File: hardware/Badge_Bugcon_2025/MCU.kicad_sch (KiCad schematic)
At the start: 62 parts, among them J1 Conn_01x21, J13 ETH, J14 Conn_01x24, J5 3V3, J8 Conn_01x24, SW2 SW_Push, SW3 SW_Push, U6 W25N02KVZEIR, Y1 Crystal, Y2 24MHz

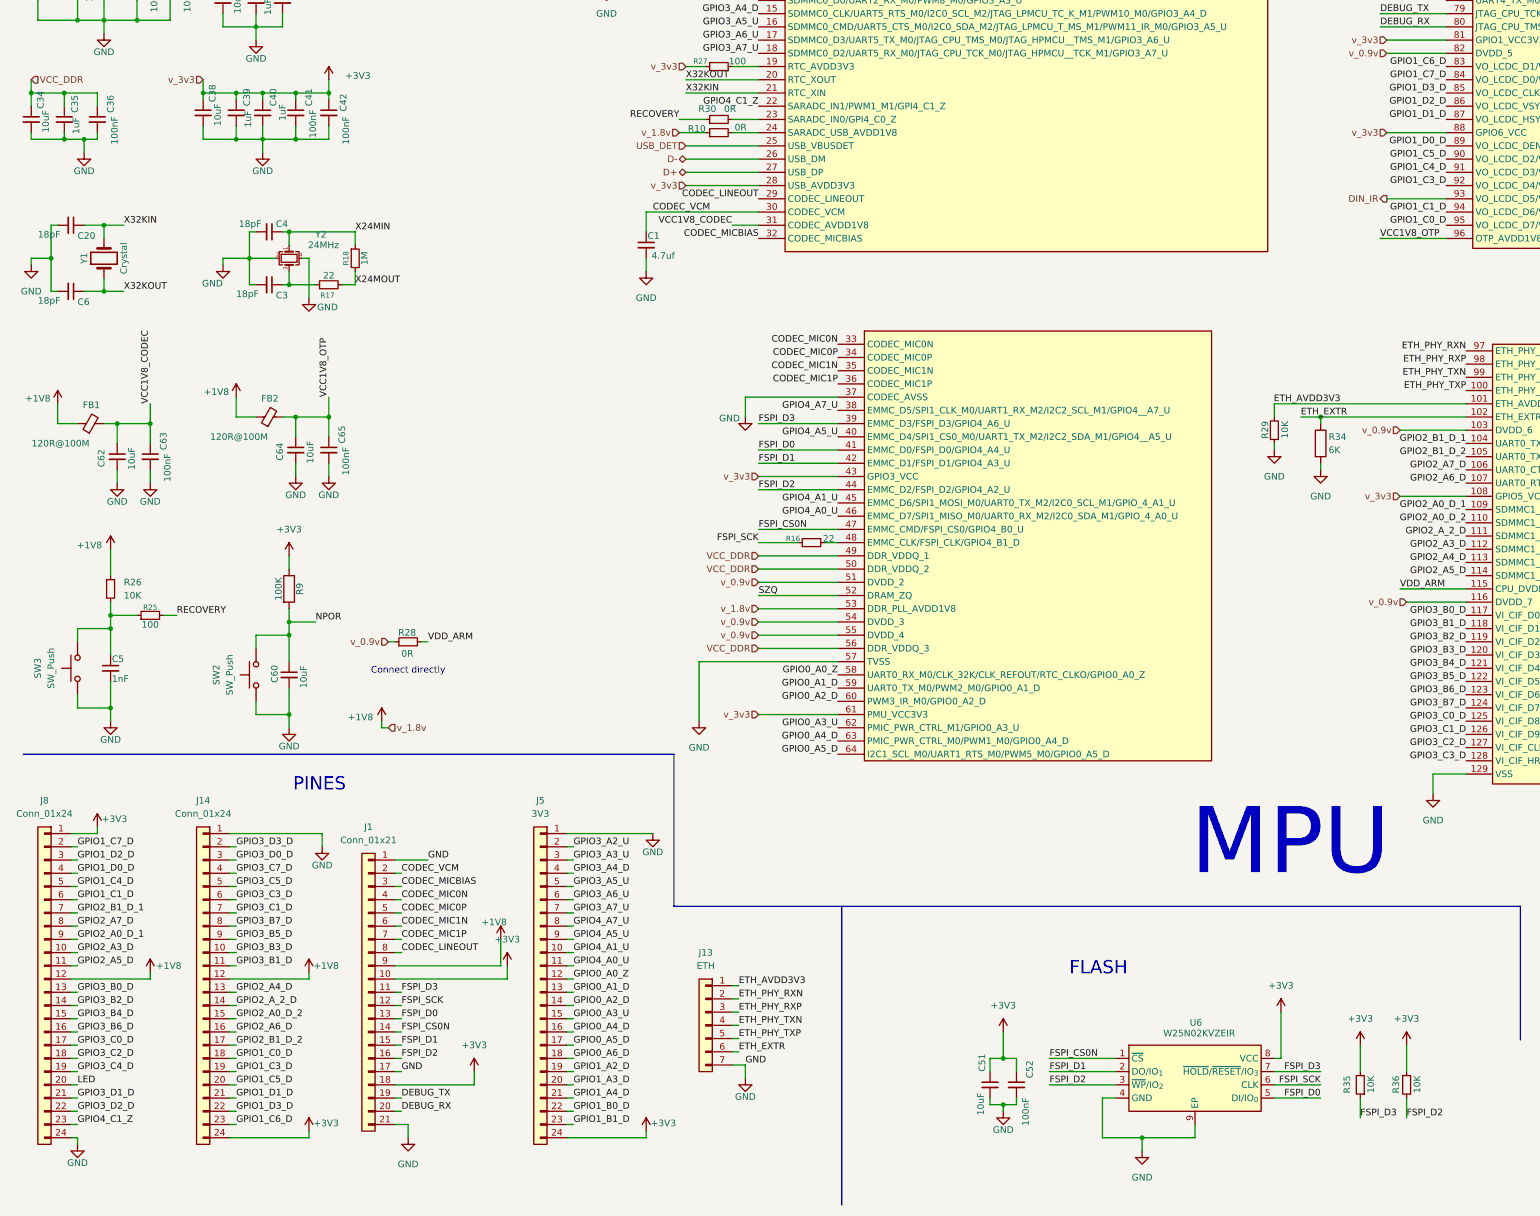
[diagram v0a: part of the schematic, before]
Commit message: feat(Hw):Update_Schaematic_And_BOM
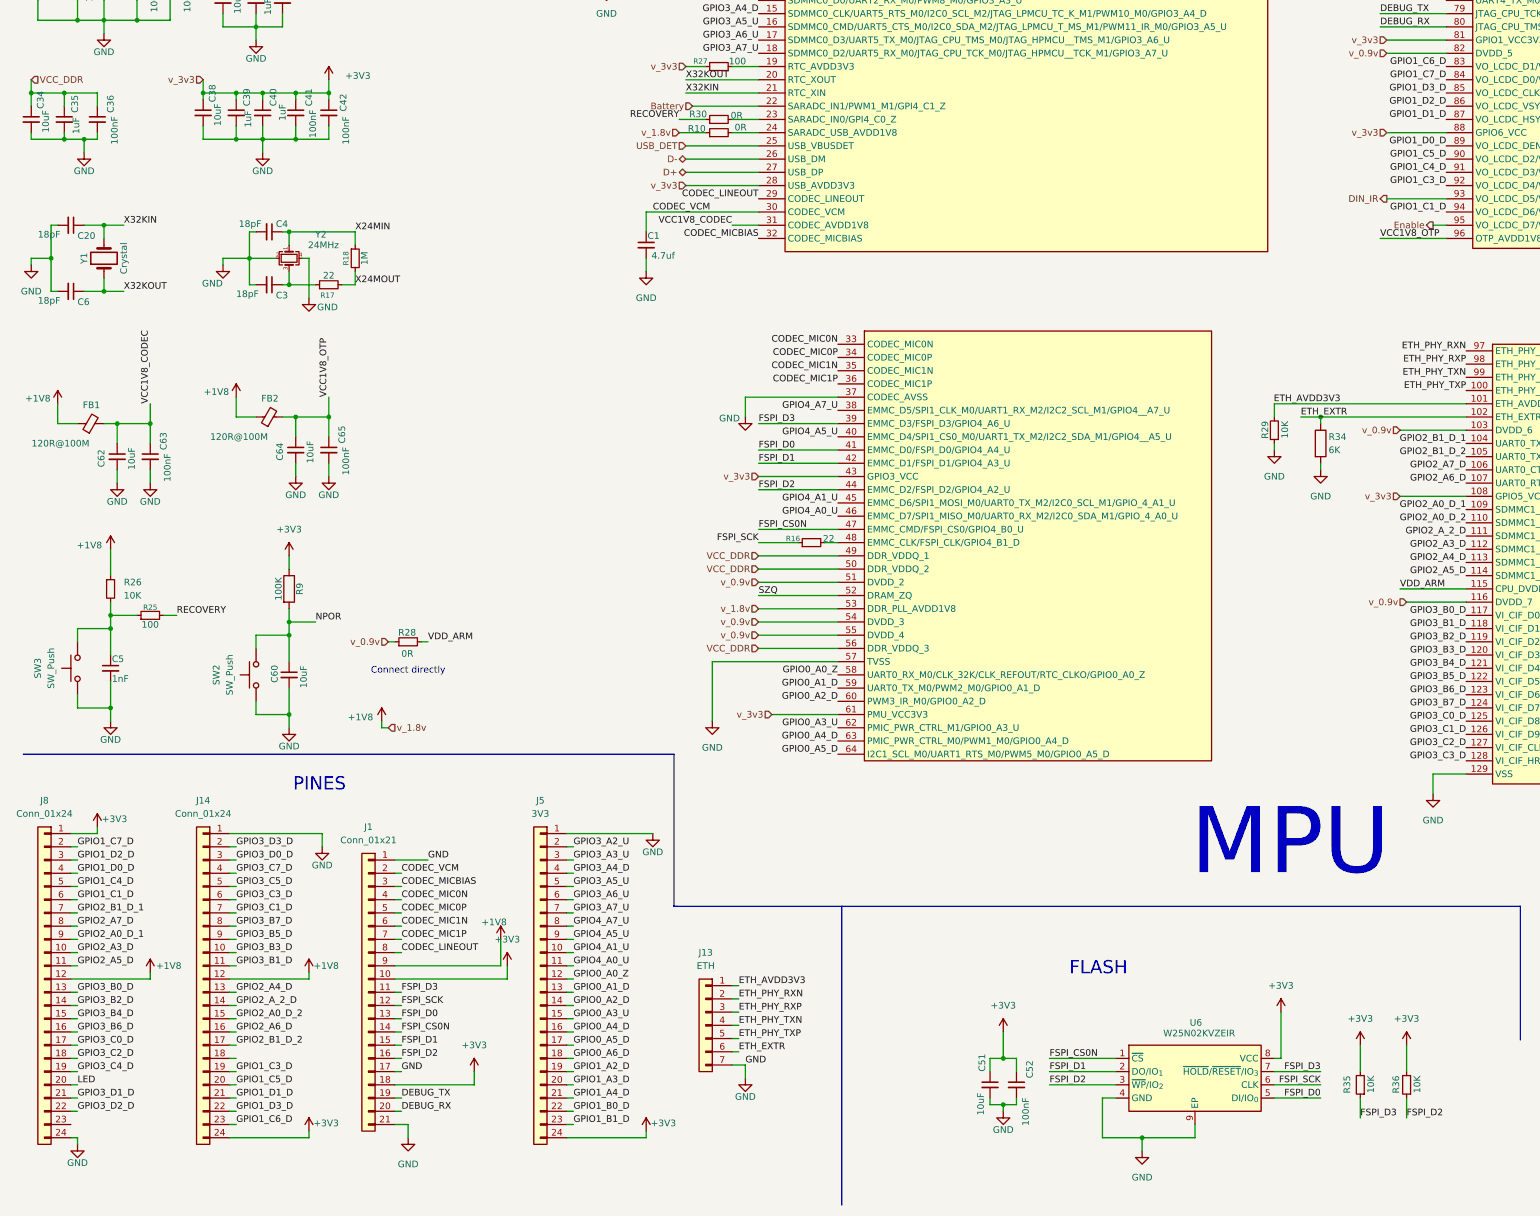
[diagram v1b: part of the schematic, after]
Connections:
- net GPIO1_C0_D: no longer names the net of J14.18 (Pin_18)
- net GPIO1_C0_D: no longer U8.95 (VO_LCDC_D7/VI_CIF_D2_M1/PWM2_M2/SPI0_CS0_M0/_SDMMC1_D1_M1/GPIO1_C0_D)
- net GPIO4_C1_Z: no longer names the net of J8.23 (Pin_23)
- net GPIO4_C1_Z: no longer U8.22 (SARADC_IN1/PWM1_M1/GPI4_C1_Z)
- new net Battery: U8.22 (SARADC_IN1/PWM1_M1/GPI4_C1_Z)
- new net Enable: U8.95 (VO_LCDC_D7/VI_CIF_D2_M1/PWM2_M2/SPI0_CS0_M0/_SDMMC1_D1_M1/GPIO1_C0_D)

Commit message: feat(Hw):Update_Schematic_And_Route
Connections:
- net GPIO3_A2_U: no longer U8.12 (SDMMC0_D1/UART2_TX_M0/PWM9_M0/GPIO3_A2_U)
- net GPIO1_B1_D: no longer names the net of J5.23 (Pin_23)
- net GPIO1_B1_D: no longer U8.78 (UART4_TX_M0/PWM7_IR_M1/SPI1_CS1_M0/VI_CIF_D1__M1/GPIO1_B1_D)
- new net PB1: U8.78 (UART4_TX_M0/PWM7_IR_M1/SPI1_CS1_M0/VI_CIF_D1__M1/GPIO1_B1_D)
- new net PB2: U8.12 (SDMMC0_D1/UART2_TX_M0/PWM9_M0/GPIO3_A2_U)
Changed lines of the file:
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@@
 	(wire
 		(pts
+			(xy 147.32 48.26) (xy 153.67 48.26)
+		)
+		(stroke
+			(width 0)
+			(type default)
+		)
+	)
+	(wire
+		(pts
 			(xy 64.77 77.47) (xy 64.77 80.01)
 		)
@@
 	(wire
 		(pts
+			(xy 278.13 53.34) (xy 285.75 53.34)
+		)
+		(stroke
+			(width 0)
+			(type default)
+		)
+	)
+	(wire
+		(pts
 			(xy 24.13 109.22) (xy 27.94 109.22)
 		)
@@
 		)
 	)
-	(label "GPIO1_B1_D"
-		(at 285.75 53.34 180)
-		(effects
-			(font
-				(size 1.27 1.27)
-			)
-			(justify right bottom)
-		)
-	)
 	(label "GPIO0_A0_Z"
 		(at 118.11 241.3 0)
@@
 		)
 	)
-	(label "GPIO1_B1_D"
-		(at 118.11 269.24 0)
-		(effects
-			(font
-				(size 1.27 1.27)
-			)
-			(justify left bottom)
-		)
-	)
 	(label "GPIO3_B3_D"
 		(at 289.56 179.07 180)
@@
 		)
 	)
-	(label "GPIO3_A2_U"
-		(at 153.67 48.26 180)
-		(effects
-			(font
-				(size 1.27 1.27)
-			)
-			(justify right bottom)
-		)
-	)
 	(label "GPIO1_A4_D"
 		(at 285.75 48.26 180)
@@
 		)
 	)
+	(hierarchical_label "PB2"
+		(shape input)
+		(at 147.32 48.26 180)
+		(effects
+			(font
+				(size 1.27 1.27)
+			)
+			(justify right)
+		)
+	)
 	(hierarchical_label "v_0.9v"
 		(shape input)
@@
 		(effects
 			(font
+				(size 1.27 1.27)
+			)
+			(justify right)
+		)
+	)
+	(hierarchical_label "PB1"
+		(shape input)
+		(at 278.13 53.34 180)
+		(effects
+			(font

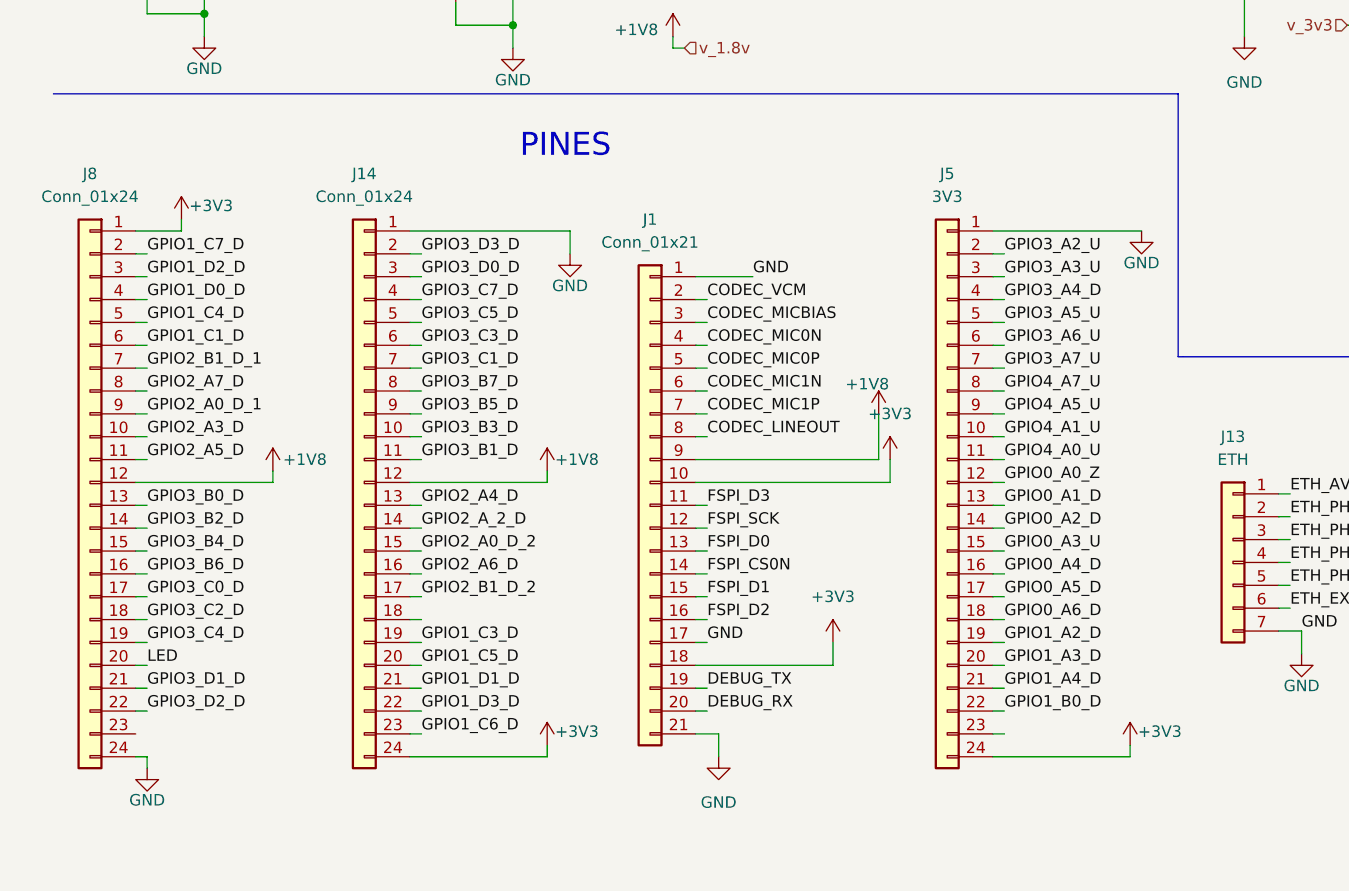
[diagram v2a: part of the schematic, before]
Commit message: feat(Hw):Update_Route_And_Schematic
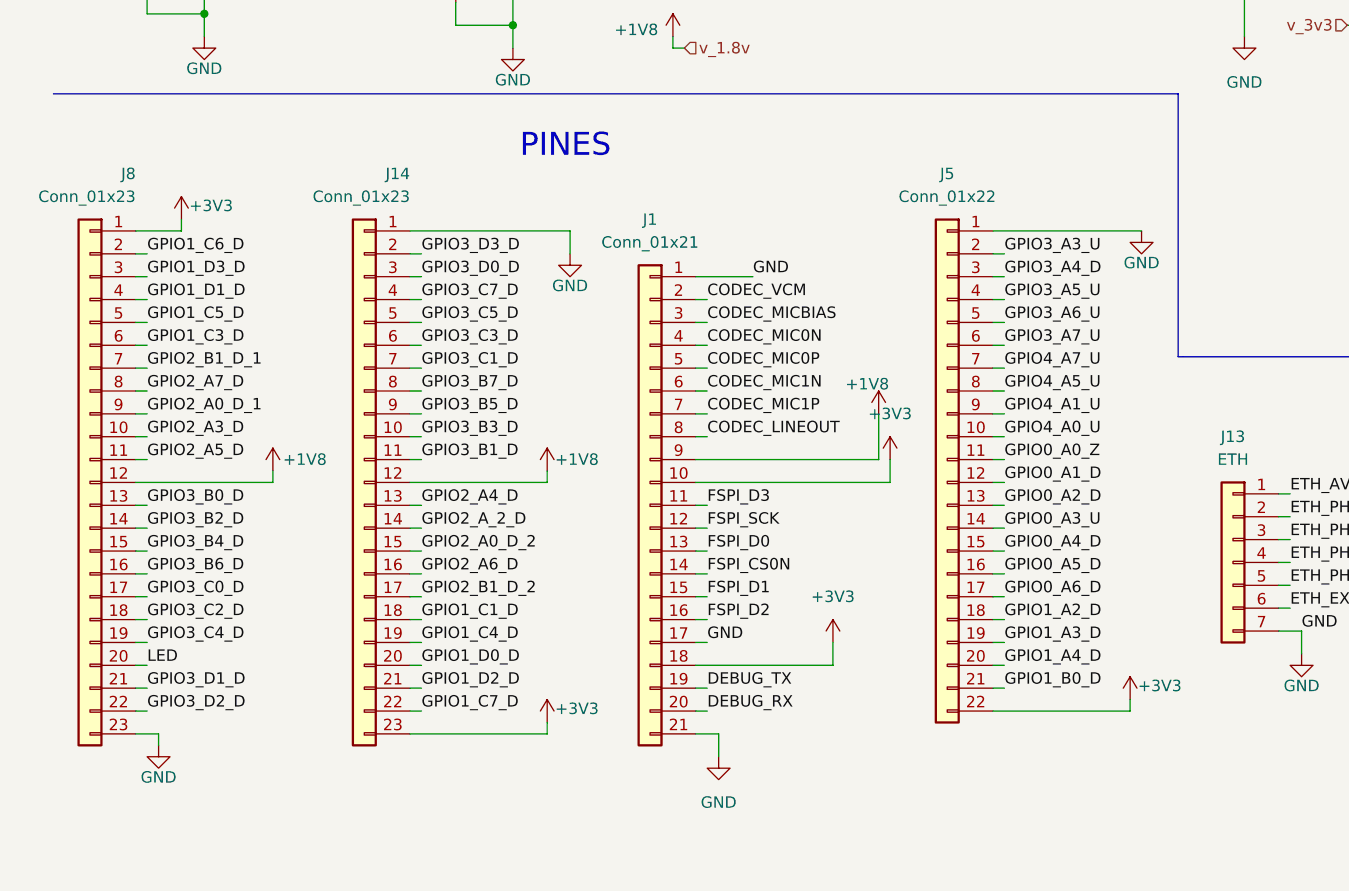
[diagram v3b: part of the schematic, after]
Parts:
- removed J14, J8: Conn_01x24, Connector_PinHeader_2.54mm:PinHeader_1x24_P2.54mm_Vertical, symbol Connector_Generic:Conn_01x24
- removed J5: 3V3, Connector_PinHeader_2.54mm:PinHeader_1x24_P2.54mm_Vertical, symbol Connector_Generic:Conn_01x24
- added J14, J8: Conn_01x23, Connector_PinHeader_2.54mm:PinHeader_1x23_P2.54mm_Vertical, symbol Connector_Generic:Conn_01x23
- added J5: Conn_01x22, Connector_PinHeader_2.54mm:PinHeader_1x22_P2.54mm_Vertical, symbol Connector_Generic:Conn_01x22
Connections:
- net +1V8: now also J14.12 (Pin_12), J8.12 (Pin_12)
- net +3V3: now also J14.23 (Pin_23), J5.22 (Pin_22), J8.1 (Pin_1)
- net GND: now also J14.1 (Pin_1), J5.1 (Pin_1), J8.23 (Pin_23)
- net GPIO0_A0_Z: now also J5.11 (Pin_11)
- net GPIO0_A1_D: now also J5.12 (Pin_12)
- net GPIO0_A2_D: now also J5.13 (Pin_13)
- net GPIO0_A3_U: now also J5.14 (Pin_14)
- net GPIO0_A4_D: now also J5.15 (Pin_15)
- net GPIO0_A5_D: now also J5.16 (Pin_16)
- net GPIO0_A6_D: now also J5.17 (Pin_17)
- net GPIO1_A2_D: now also J5.18 (Pin_18)
- net GPIO1_A3_D: now also J5.19 (Pin_19)
- net GPIO1_A4_D: now also J5.20 (Pin_20)
- net GPIO1_B0_D: now also J5.21 (Pin_21)
- net GPIO1_C1_D: now also J14.18 (Pin_18)
- net GPIO1_C3_D: now also J8.6 (Pin_6)
- net GPIO1_C4_D: now also J14.19 (Pin_19)
- net GPIO1_C5_D: now also J8.5 (Pin_5)
- net GPIO1_C6_D: now also J8.2 (Pin_2)
- net GPIO1_C7_D: now also J14.22 (Pin_22)
- net GPIO1_D0_D: now also J14.20 (Pin_20)
- net GPIO1_D1_D: now also J8.4 (Pin_4)
- net GPIO1_D2_D: now also J14.21 (Pin_21)
- net GPIO1_D3_D: now also J8.3 (Pin_3)
- net GPIO2_A0_D_1: now also J8.9 (Pin_9)
- net GPIO2_A0_D_2: now also J14.15 (Pin_15)
- net GPIO2_A3_D: now also J8.10 (Pin_10)
- net GPIO2_A4_D: now also J14.13 (Pin_13)
- net GPIO2_A5_D: now also J8.11 (Pin_11)
- net GPIO2_A6_D: now also J14.16 (Pin_16)
- net GPIO2_A7_D: now also J8.8 (Pin_8)
- net GPIO2_A_2_D: now also J14.14 (Pin_14)
- net GPIO2_B1_D_1: now also J8.7 (Pin_7)
- net GPIO2_B1_D_2: now also J14.17 (Pin_17)
- net GPIO3_A3_U: now also J5.2 (Pin_2)
- net GPIO3_A4_D: now also J5.3 (Pin_3)
- net GPIO3_A5_U: now also J5.4 (Pin_4)
- net GPIO3_A6_U: now also J5.5 (Pin_5)
- net GPIO3_A7_U: now also J5.6 (Pin_6)
- net GPIO3_B0_D: now also J8.13 (Pin_13)
- net GPIO3_B1_D: now also J14.11 (Pin_11)
- net GPIO3_B2_D: now also J8.14 (Pin_14)
- net GPIO3_B3_D: now also J14.10 (Pin_10)
- net GPIO3_B4_D: now also J8.15 (Pin_15)
- net GPIO3_B5_D: now also J14.9 (Pin_9)
- net GPIO3_B6_D: now also J8.16 (Pin_16)
- net GPIO3_B7_D: now also J14.8 (Pin_8)
- net GPIO3_C0_D: now also J8.17 (Pin_17)
- net GPIO3_C1_D: now also J14.7 (Pin_7)
- net GPIO3_C2_D: now also J8.18 (Pin_18)
- net GPIO3_C3_D: now also J14.6 (Pin_6)
- net GPIO3_C4_D: now also J8.19 (Pin_19)
- net GPIO3_C5_D: now also J14.5 (Pin_5)
- net GPIO3_C7_D: now also J14.4 (Pin_4)
- net GPIO3_D0_D: now also J14.3 (Pin_3)
- net GPIO3_D1_D: now also J8.21 (Pin_21)
- net GPIO3_D2_D: now also J8.22 (Pin_22)
- net GPIO3_D3_D: now also J14.2 (Pin_2)
- net GPIO4_A0_U: now also J5.10 (Pin_10)
- net GPIO4_A1_U: now also J5.9 (Pin_9)
- net GPIO4_A5_U: now also J5.8 (Pin_8)
- net GPIO4_A7_U: now also J5.7 (Pin_7)
- net LED: now also J8.20 (Pin_20)

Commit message: feat(Hw):Update_Route
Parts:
- SW2, SW3: footprint Footprints:TS1088R02026 -> Button_Switch_SMD:SW_SPST_TL3342; LCSC# C455281 -> C318889
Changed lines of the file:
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@@
 			)
 		)
-		(property "Footprint" "Footprints:TS1088R02026"
+		(property "Footprint" "Button_Switch_SMD:SW_SPST_TL3342"
 			(at 17.78 181.61 0)
 			(effects
@@
 			)
 		)
-		(property "LCSC#" "C455281"
+		(property "LCSC#" "C318889"
 			(at 22.86 181.61 0)
 			(effects
@@
 			)
 		)
-		(property "Footprint" "Footprints:TS1088R02026"
+		(property "Footprint" "Button_Switch_SMD:SW_SPST_TL3342"
 			(at 52.07 182.88 0)
 			(effects
@@
 			)
 		)
-		(property "LCSC#" "C455281"
+		(property "LCSC#" "C318889"
 			(at 57.15 182.88 0)
 			(effects
